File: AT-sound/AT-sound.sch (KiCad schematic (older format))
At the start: 18 parts

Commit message: started layout and routing!
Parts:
- removed Q?: 2N7000, Package_TO_SOT_THT:TO-92_Inline, symbol Transistor_FET:2N7000
- added Q1: AQY212S, Package_TO_SOT_SMD:SOT-23, symbol Device:Q_NMOS_GSD
- added TP1: 5v, TestPoint:TestPoint_Pad_D1.0mm, symbol Connector:TestPoint
- added TP2: GND, TestPoint:TestPoint_Pad_D1.0mm, symbol Connector:TestPoint
- added TP3: RESET, TestPoint:TestPoint_Pad_D1.0mm, symbol Connector:TestPoint
- added TP4: SKL, TestPoint:TestPoint_Pad_D1.0mm, symbol Connector:TestPoint
- added TP5: MISO, TestPoint:TestPoint_Pad_D1.0mm, symbol Connector:TestPoint
- added TP6: MOSI, TestPoint:TestPoint_Pad_D1.0mm, symbol Connector:TestPoint
- J1: renamed from J?; footprint (none) -> Connector_PinSocket_2.54mm:PinSocket_1x02_P2.54mm_Vertical
- J2, J3: renamed from J?; footprint (none) -> Connector_PinSocket_2.54mm:PinSocket_1x03_P2.54mm_Vertical
- R1, R2, R3, R4, R5, R6: renamed from R?; footprint (none) -> Resistor_SMD:R_0603_1608Metric
- U2, U3: renamed from U?; footprint Package_DIP:DIP-4_W10.16mm -> Package_SO:SOP-4_3.8x4.1mm_P2.54mm
- gave numbers to parts that had none: 6
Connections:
- net +5V: now also TP1.1
- net GND: now also J2.1 (Pin_1), J3.1 (Pin_1), Q1.2 (S), TP2.1
- net Relay: now also Q1.1 (G)
- net at U1.4 (~RESET~/PB3): now also TP3.1
- net at U1.7 (PA6): now also TP6.1
- net at U1.8 (PA5): now also TP5.1
- net at U1.9 (PA4): now also TP4.1
- net at R5.2, R6.2: now also Q1.3 (D)

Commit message: did a little routing
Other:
- note added: "opto cupler part number wrong."
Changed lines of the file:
@@
 Wire Wire Line
 	2900 4050 2900 4100
+Text Notes 6550 2550 0    50   ~ 0
+opto cupler part number wrong.
 $EndSCHEMATC

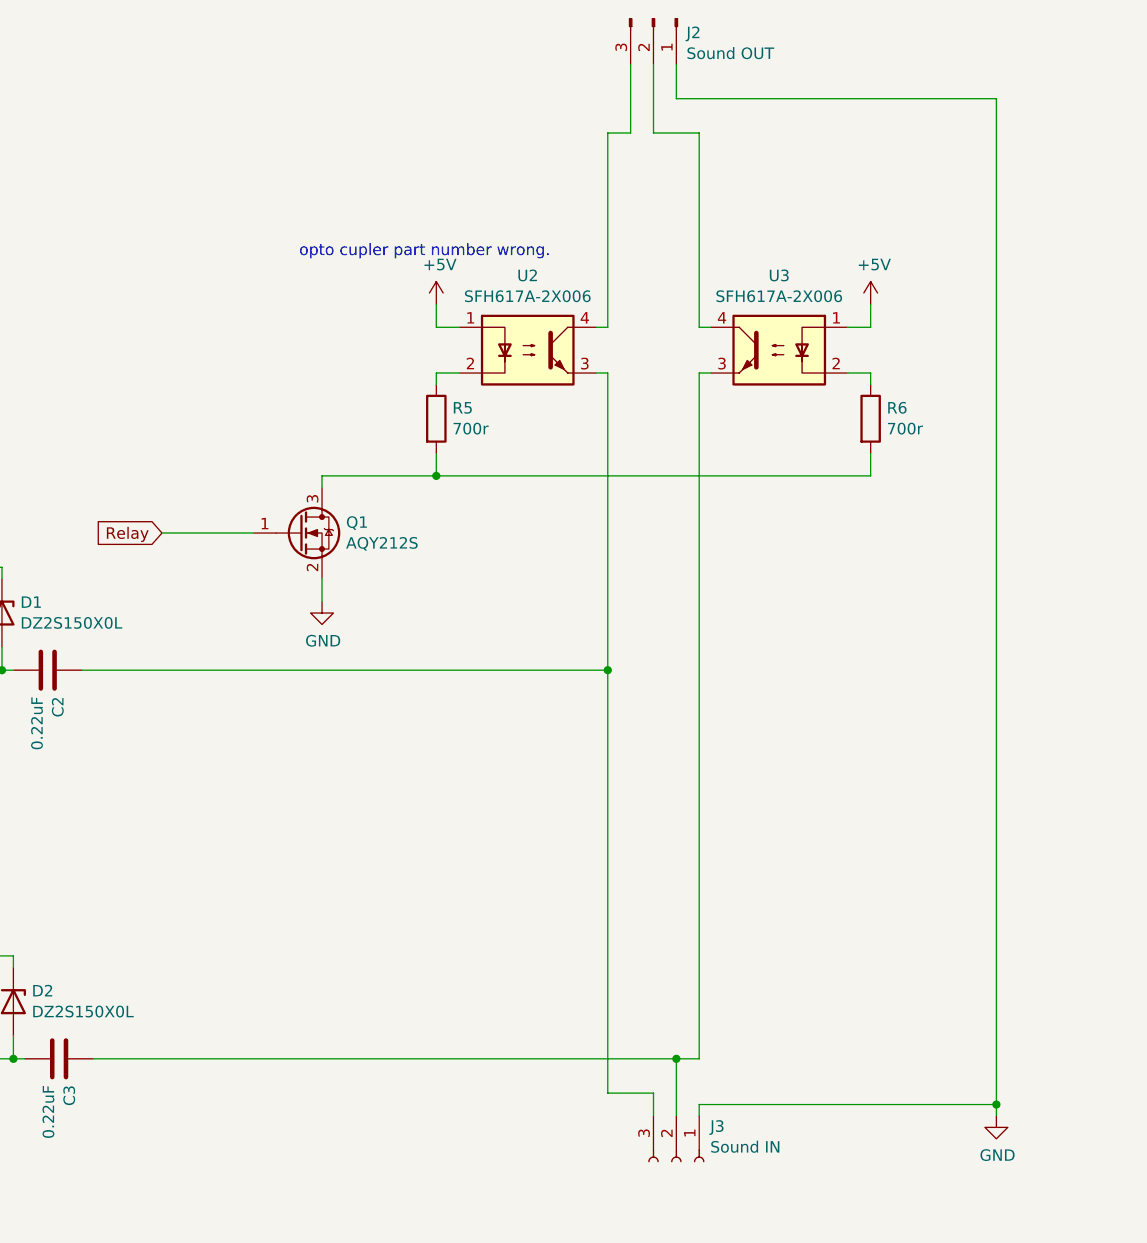
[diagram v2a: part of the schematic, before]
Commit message: made a external realay verant.
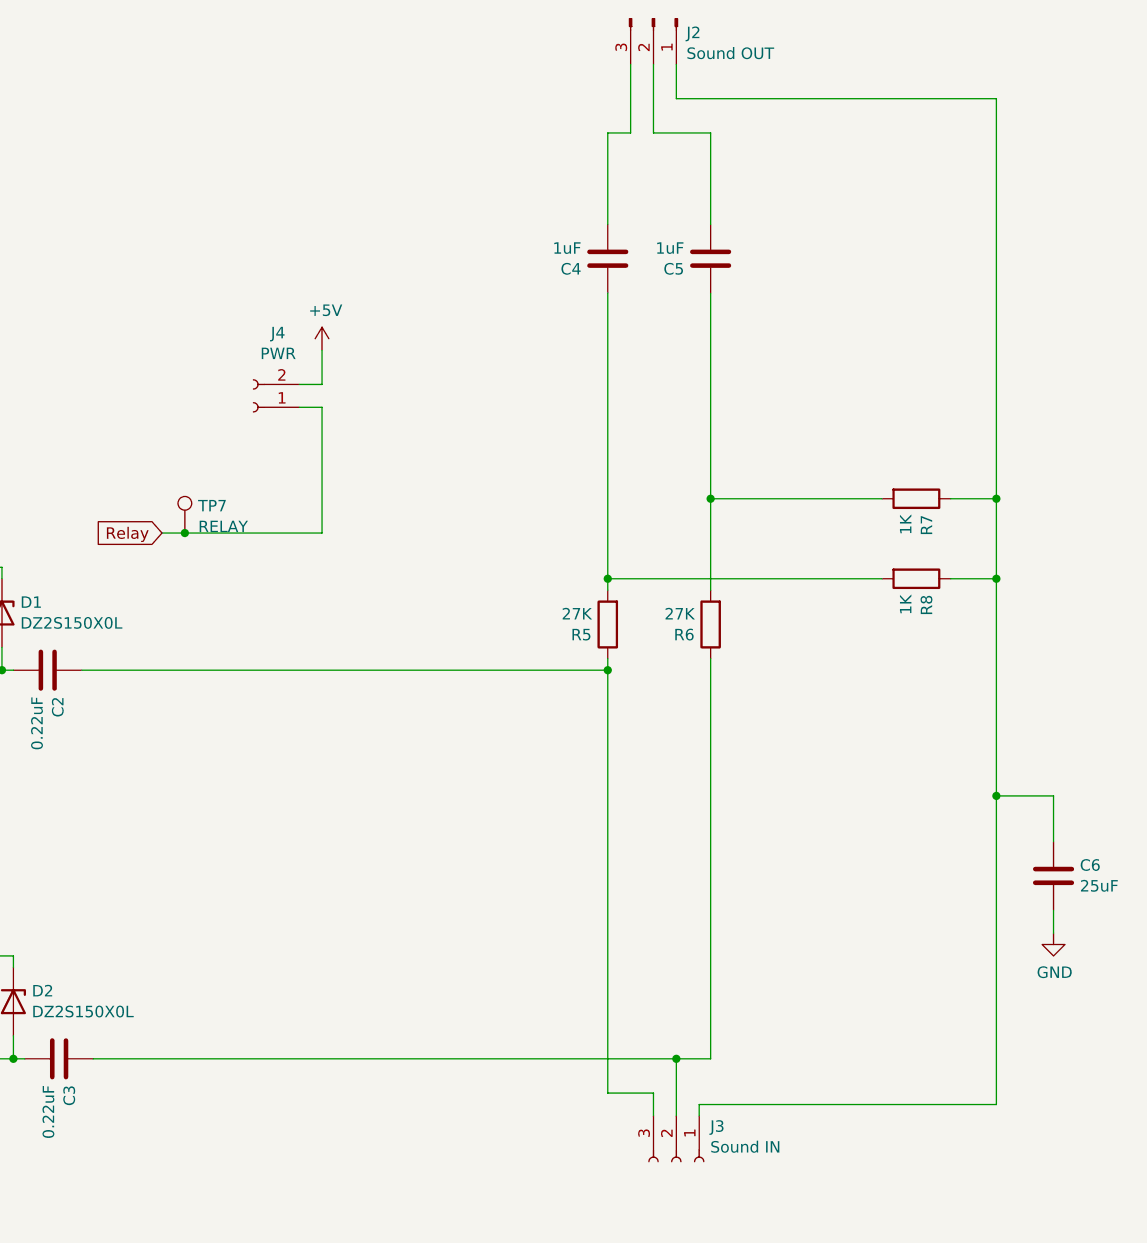
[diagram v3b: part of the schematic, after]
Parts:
- removed Q1: AQY212S, Package_TO_SOT_SMD:SOT-23, symbol Device:Q_NMOS_GSD
- removed U2, U3: SFH617A-2X006, Package_SO:SOP-4_3.8x4.1mm_P2.54mm, symbol Isolator:SFH617A-2X006
- added C4, C5: 1uF, Capacitor_SMD:C_0805_2012Metric, symbol Device:C
- added C6: 25uF, Capacitor_SMD:C_0805_2012Metric, symbol Device:C
- added J4: PWR, Connector_PinSocket_2.54mm:PinSocket_1x02_P2.54mm_Vertical, symbol Connector:Conn_01x02_Female
- added R7, R8: 1K, Resistor_SMD:R_0603_1608Metric, symbol Device:R
- added TP7: RELAY, TestPoint:TestPoint_Pad_D1.0mm, symbol Connector:TestPoint
- R5, R6: value 700r -> 27K
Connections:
- net +5V: now also J4.2 (Pin_2)
- net GND: now also C6.2; no longer J2.1 (Pin_1), J3.1 (Pin_1)
- net Relay: now also J4.1 (Pin_1), TP7.1
- net at C2.1, J3.3 (Pin_3): now also R5.1
- net at C3.1, J3.2 (Pin_2): now also R6.1
- net at J2.2 (Pin_2): now also C5.2
- net at J2.3 (Pin_3): now also C4.2
- net at R5.2: now also C4.1, R8.2; no longer R6.2
- new net: C6.1, J2.1 (Pin_1), J3.1 (Pin_1), R7.1, R8.1
- new net: C5.1, R6.2, R7.2
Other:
- note removed: "opto cupler part number wrong."
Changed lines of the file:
@@
 Wire Wire Line
 	1250 2900 1250 2850
-$Comp
-L power:+5V #PWR0105
-U 1 1 60945321
-P 7150 2750
-F 0 "#PWR0105" H 7150 2600 50  0001 C CNN
-F 1 "+5V" H 7165 2923 50  0000 C CNN
-F 2 "" H 7150 2750 50  0001 C CNN
-F 3 "" H 7150 2750 50  0001 C CNN
-	1    7150 2750
-	1    0    0    -1
-$EndComp
-$Comp
-L power:GND #PWR0106
-U 1 1 6094659F
-P 6650 4050
-F 0 "#PWR0106" H 6650 3800 50  0001 C CNN
-F 1 "GND" H 6655 3877 50  0000 C CNN
-F 2 "" H 6650 4050 50  0001 C CNN
-F 3 "" H 6650 4050 50  0001 C CNN
-	1    6650 4050
-	1    0    0    -1
-$EndComp
-Wire Wire Line
-	6650 4050 6650 3950
 Text GLabel 5950 3750 0    50   Input ~ 0
 Relay
 Wire Wire Line
-	5950 3750 6350 3750
+	5950 3750 6050 3750
 Text GLabel 3750 2700 2    50   Input ~ 0
 Relay
@@
 	8100 1700 8100 2000
 Wire Wire Line
-	8100 2000 8300 2000
-Wire Wire Line
 	7900 2000 8000 2000
 Wire Wire Line
@@
 	1600 4800 1600 4900
 Wire Wire Line
-	7150 2750 7150 2850
-$Comp
-L Device:R R5
-U 1 1 609C95CA
-P 7150 3250
-F 0 "R5" H 7220 3296 50  0000 L CNN
-F 1 "700r" H 7220 3205 50  0000 L CNN
-F 2 "Resistor_SMD:R_0603_1608Metric" V 7080 3250 50  0001 C CNN
-F 3 "~" H 7150 3250 50  0001 C CNN
-	1    7150 3250
-	1    0    0    -1
-$EndComp
-$Comp
-L Isolator:SFH617A-2X006 U2
-U 1 1 609CB032
-P 7550 2950
-F 0 "U2" H 7550 3275 50  0000 C CNN
-F 1 "SFH617A-2X006" H 7550 3184 50  0000 C CNN
-F 2 "Package_SO:SOP-4_3.8x4.1mm_P2.54mm" H 7350 2750 50  0001 L CIN
-F 3 "http://www.vishay.com/docs/83740/sfh617a.pdf" H 7550 2950 50  0001 L CNN
-	1    7550 2950
-	1    0    0    -1
-$EndComp
-$Comp
-L power:+5V #PWR0113
-U 1 1 609CF039
-P 9050 2750
-F 0 "#PWR0113" H 9050 2600 50  0001 C CNN
-F 1 "+5V" H 9065 2923 50  0000 C CNN
-F 2 "" H 9050 2750 50  0001 C CNN
-F 3 "" H 9050 2750 50  0001 C CNN
-	1    9050 2750
-	1    0    0    -1
-$EndComp
-Wire Wire Line
-	9050 2750 9050 2850
-$Comp
-L Isolator:SFH617A-2X006 U3
-U 1 1 609CF040
-P 8650 2950
-F 0 "U3" H 8650 3275 50  0000 C CNN
-F 1 "SFH617A-2X006" H 8650 3184 50  0000 C CNN
-F 2 "Package_SO:SOP-4_3.8x4.1mm_P2.54mm" H 8450 2750 50  0001 L CIN
-F 3 "http://www.vishay.com/docs/83740/sfh617a.pdf" H 8650 2950 50  0001 L CNN
-	1    8650 2950
-	-1   0    0    -1
-$EndComp
-$Comp
-L Device:R R6
-U 1 1 609D1D65
-P 9050 3250
-F 0 "R6" H 9120 3296 50  0000 L CNN
-F 1 "700r" H 9120 3205 50  0000 L CNN
-F 2 "Resistor_SMD:R_0603_1608Metric" V 8980 3250 50  0001 C CNN
-F 3 "~" H 9050 3250 50  0001 C CNN
-	1    9050 3250
-	1    0    0    -1
-$EndComp
-Wire Wire Line
-	7850 2850 7900 2850
-Wire Wire Line
-	7900 2000 7900 2850
-Wire Wire Line
-	7850 3050 7900 3050
-Wire Wire Line
-	7900 3050 7900 4350
-Wire Wire Line
 	7900 6200 8100 6200
 Wire Wire Line
@@
 Wire Wire Line
 	5600 4350 7900 4350
-Connection ~ 7900 4350
 Wire Wire Line
 	7900 4350 7900 6200
-Wire Wire Line
-	8350 3050 8300 3050
-Wire Wire Line
-	8300 3050 8300 6050
-Wire Wire Line
-	8300 6050 8200 6050
 Connection ~ 8200 6050
 Wire Wire Line
-	8300 2850 8350 2850
-Wire Wire Line
-	8300 2000 8300 2850
-Wire Wire Line
-	8950 3050 9050 3050
-Wire Wire Line
-	9050 3050 9050 3100
-Wire Wire Line
-	7150 3050 7150 3100
-Wire Wire Line
-	7150 3050 7250 3050
-Wire Wire Line
-	6650 3500 6650 3550
-Wire Wire Line
-	6650 3500 7150 3500
-Wire Wire Line
-	9050 3500 9050 3400
-Wire Wire Line
-	7150 3400 7150 3500
-Connection ~ 7150 3500
-Wire Wire Line
-	7150 3500 9050 3500
-Wire Wire Line
-	8950 2850 9050 2850
-Wire Wire Line
-	7250 2850 7150 2850
-Wire Wire Line
 	3500 2500 3650 2500
 Wire Wire Line
@@
 	3750 2700 3500 2700
 Wire Wire Line
-	9600 1850 9600 6250
+	9600 1850 9600 3600
 Wire Wire Line
 	8200 1850 9600 1850
@@
 L power:GND #PWR0114
 U 1 1 60A3AA5E
-P 9600 6300
-F 0 "#PWR0114" H 9600 6050 50  0001 C CNN
-F 1 "GND" H 9605 6127 50  0000 C CNN
-F 2 "" H 9600 6300 50  0001 C CNN
-F 3 "" H 9600 6300 50  0001 C CNN
-	1    9600 6300
-	1    0    0    -1
-$EndComp
-Connection ~ 9600 6250
-Wire Wire Line
-	9600 6300 9600 6250
-$Comp
-L Device:Q_NMOS_GSD Q1
-U 1 1 60A53CA3
-P 6550 3750
-F 0 "Q1" H 6755 3796 50  0000 L CNN
-F 1 "AQY212S" H 6755 3705 50  0000 L CNN
-F 2 "Package_TO_SOT_SMD:SOT-23" H 6750 3850 50  0001 C CNN
-F 3 "~" H 6550 3750 50  0001 C CNN
-	1    6550 3750
+P 9850 5500
+F 0 "#PWR0114" H 9850 5250 50  0001 C CNN
+F 1 "GND" H 9855 5327 50  0000 C CNN
+F 2 "" H 9850 5500 50  0001 C CNN
+F 3 "" H 9850 5500 50  0001 C CNN
+	1    9850 5500
 	1    0    0    -1
 $EndComp
@@
 Wire Wire Line
 	2900 4050 2900 4100
-Text Notes 6550 2550 0    50   ~ 0
-opto cupler part number wrong.
+$Comp
+L Connector:TestPoint TP7
+U 1 1 609729FE
+P 6050 3750
+F 0 "TP7" H 6108 3868 50  0000 L CNN
+F 1 "RELAY" H 6108 3777 50  0000 L CNN
+F 2 "TestPoint:TestPoint_Pad_D1.0mm" H 6250 3750 50  0001 C CNN
+F 3 "~" H 6250 3750 50  0001 C CNN
+	1    6050 3750
+	1    0    0    -1
+$EndComp
+Connection ~ 6050 3750
+$Comp
+L power:+5V #PWR0105
+U 1 1 609AED36
+P 6650 2950
+F 0 "#PWR0105" H 6650 2800 50  0001 C CNN
+F 1 "+5V" H 6665 3123 50  0000 C CNN
+F 2 "" H 6650 2950 50  0001 C CNN
+F 3 "" H 6650 2950 50  0001 C CNN
+	1    6650 2950
+	1    0    0    -1
+$EndComp
+$Comp
+L Connector:Conn_01x02_Female J4
+U 1 1 609B00EC
+P 6350 3200
+F 0 "J4" H 6242 2875 50  0000 C CNN
+F 1 "PWR" H 6242 2966 50  0000 C CNN
+F 2 "Connector_PinSocket_2.54mm:PinSocket_1x02_P2.54mm_Vertical" H 6350 3200 50  0001 C CNN
+F 3 "~" H 6350 3200 50  0001 C CNN
+	1    6350 3200
+	-1   0    0    1
+$EndComp
+Wire Wire Line
+	6550 3200 6650 3200
+Wire Wire Line
+	6550 3100 6650 3100
+Wire Wire Line
+	6650 3100 6650 2950
+Wire Wire Line
+	6050 3750 6650 3750
+Wire Wire Line
+	6650 3200 6650 3750
+$Comp
+L Device:R R8
+U 1 1 609A2CC8
+P 9250 3950
+F 0 "R8" H 9320 3996 50  0000 L CNN
+F 1 "1K" H 9320 3905 50  0000 L CNN
+F 2 "Resistor_SMD:R_0603_1608Metric" V 9180 3950 50  0001 C CNN
+F 3 "~" H 9250 3950 50  0001 C CNN
+	1    9250 3950
+	0    1    1    0
+$EndComp
+$Comp
+L Device:R R7
+U 1 1 609A3959
+P 9250 3600
+F 0 "R7" H 9320 3646 50  0000 L CNN
+F 1 "1K" H 9320 3555 50  0000 L CNN
+F 2 "Resistor_SMD:R_0603_1608Metric" V 9180 3600 50  0001 C CNN
+F 3 "~" H 9250 3600 50  0001 C CNN
+	1    9250 3600
+	0    1    1    0
+$EndComp
+Wire Wire Line
+	9400 3600 9600 3600
+Connection ~ 9600 3600
+Wire Wire Line
+	9600 3600 9600 3950
+Wire Wire Line
+	9400 3950 9600 3950
+Connection ~ 9600 3950
+Wire Wire Line
+	9600 3950 9600 4900
+Wire Wire Line
+	9100 3950 7900 3950
+$Comp
+L Device:R R5
+U 1 1 609AB640
+P 7900 4150
+F 0 "R5" H 7970 4196 50  0000 L CNN
+F 1 "27K" H 7970 4105 50  0000 L CNN
+F 2 "Resistor_SMD:R_0603_1608Metric" V 7830 4150 50  0001 C CNN
+F 3 "~" H 7900 4150 50  0001 C CNN
+	1    7900 4150
+	-1   0    0    1
+$EndComp
+$Comp
+L Device:R R6
+U 1 1 609AB907
+P 8350 4150
+F 0 "R6" H 8420 4196 50  0000 L CNN
+F 1 "27K" H 8420 4105 50  0000 L CNN
+F 2 "Resistor_SMD:R_0603_1608Metric" V 8280 4150 50  0001 C CNN
+F 3 "~" H 8350 4150 50  0001 C CNN
+	1    8350 4150
+	-1   0    0    1
+$EndComp
+$Comp
+L Device:C C4
+U 1 1 609AC4E7
+P 7900 2550
+F 0 "C4" H 8015 2596 50  0000 L CNN
+F 1 "1uF" H 8015 2505 50  0000 L CNN
+F 2 "Capacitor_SMD:C_0805_2012Metric" H 7938 2400 50  0001 C CNN
+F 3 "~" H 7900 2550 50  0001 C CNN
+	1    7900 2550
+	-1   0    0    1
+$EndComp
+$Comp
+L Device:C C5
+U 1 1 609AD05A
+P 8350 2550
+F 0 "C5" H 8465 2596 50  0000 L CNN
+F 1 "1uF" H 8465 2505 50  0000 L CNN
+F 2 "Capacitor_SMD:C_0805_2012Metric" H 8388 2400 50  0001 C CNN
+F 3 "~" H 8350 2550 50  0001 C CNN
+	1    8350 2550
+	-1   0    0    1
+$EndComp
+Wire Wire Line
+	7900 2000 7900 2400
+Wire Wire Line
+	8350 2000 8350 2400
+Wire Wire Line
+	8100 2000 8350 2000
+Wire Wire Line
+	8350 2700 8350 3600
+Wire Wire Line
+	8350 3600 9100 3600
+Wire Wire Line
+	7900 2700 7900 3950
+Wire Wire Line
+	8350 6050 8350 4300
+Wire Wire Line
+	8200 6050 8350 6050
+Wire Wire Line
+	7900 4300 7900 4350
+Connection ~ 7900 4350
+Wire Wire Line
+	7900 4000 7900 3950
+Connection ~ 7900 3950
+Wire Wire Line
+	8350 4000 8350 3600
+Connection ~ 8350 3600
+$Comp
+L Device:C C6
+U 1 1 609FE072
+P 9850 5250
+F 0 "C6" H 9965 5296 50  0000 L CNN
+F 1 "25uF" H 9965 5205 50  0000 L CNN
+F 2 "Capacitor_SMD:C_0805_2012Metric" H 9888 5100 50  0001 C CNN
+F 3 "~" H 9850 5250 50  0001 C CNN
+	1    9850 5250
+	1    0    0    -1
+$EndComp
+Wire Wire Line
+	9850 5100 9850 4900
+Wire Wire Line
+	9850 4900 9600 4900
+Connection ~ 9600 4900
+Wire Wire Line
+	9600 4900 9600 6250
+Wire Wire Line
+	9850 5500 9850 5400
 $EndSCHEMATC
